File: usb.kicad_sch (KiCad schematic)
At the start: 24 parts, among them J4 CONN_02X03, U6 FT231XQ, Y1 FNETHE025

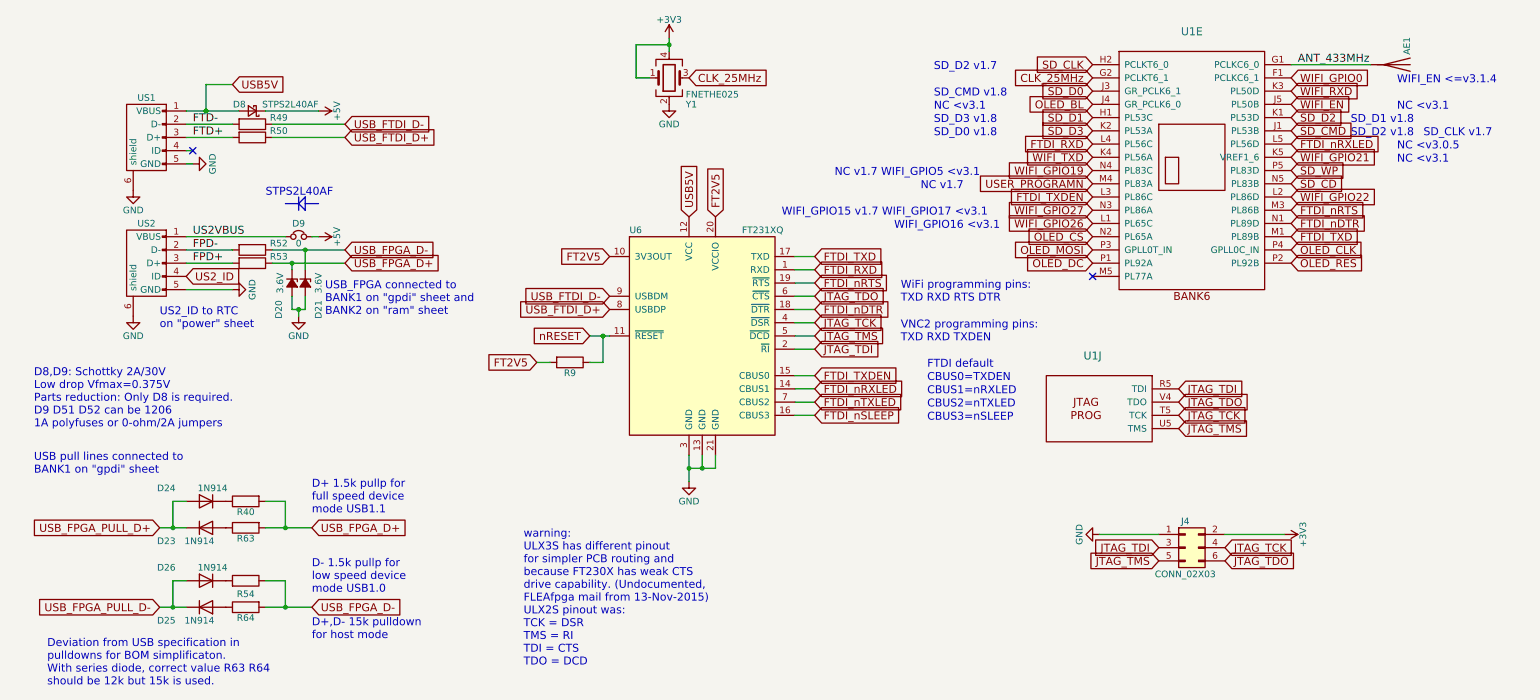
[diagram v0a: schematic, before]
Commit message: Adding USB-C
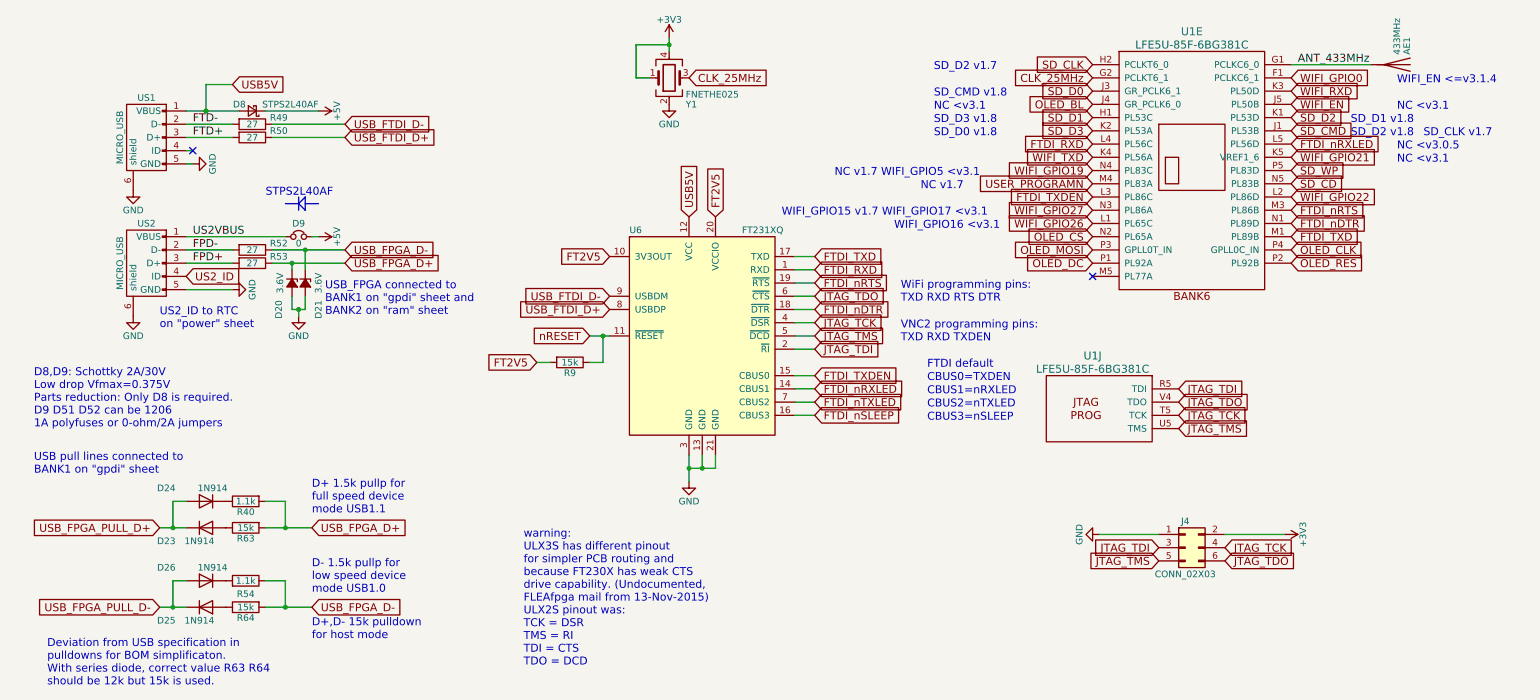
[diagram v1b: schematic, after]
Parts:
- AE1: value (none) -> 433MHz; footprint (none) -> USB-C:1013706200021LF
- J4: footprint Socket_Strips:Socket_Strip_Straight_2x03 -> Connector_PinSocket_2.54mm:PinSocket_2x03_P2.54mm_Vertical_SMD
- R40, R54: value (none) -> 1.1k; footprint (none) -> Resistor_SMD:R_0603_1608Metric
- R49, R50, R52, R53: value (none) -> 27; footprint (none) -> Resistor_SMD:R_0603_1608Metric
- R63, R64, R9: value (none) -> 15k; footprint (none) -> Resistor_SMD:R_0603_1608Metric
- U1: value (none) -> LFE5U-85F-6BG381C; footprint (none) -> lfe5bg381:BGA-381_pitch0.8mm_dia0.4mm
- US1, US2: value (none) -> MICRO_USB; footprint (none) -> usb_otg:USB-MICRO-B-FCI-10118192-0001LF
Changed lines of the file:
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@@
   (title_block
     (title "ULX3S")
-    (rev "1.0.10")
+    (date "2023-01-19")
+    (rev "3.1.8")
     (company "EMARD")
     (comment 1 "USB serial and JTAG")
@@
     (in_bom yes) (on_board yes)
     (property "Reference" "US1" (id 0) (at 38.1 40.64 90))
-    (property "Value" "" (id 1) (at 33.02 48.26 0))
-    (property "Footprint" "" (id 2) (at 40.64 46.99 90)
+    (property "Value" "MICRO_USB" (id 1) (at 33.02 48.26 0))
+    (property "Footprint" "usb_otg:USB-MICRO-B-FCI-10118192-0001LF" (id 2) (at 40.64 46.99 90)
       (effects (font (size 1.27 1.27)) hide)
     )
@@
     (in_bom yes) (on_board yes)
     (property "Reference" "US2" (id 0) (at 38.1 64.77 90))
-    (property "Value" "" (id 1) (at 33.02 72.39 0))
-    (property "Footprint" "" (id 2) (at 40.64 71.12 90)
+    (property "Value" "MICRO_USB" (id 1) (at 33.02 72.39 0))
+    (property "Footprint" "usb_otg:USB-MICRO-B-FCI-10118192-0001LF" (id 2) (at 40.64 71.12 90)
       (effects (font (size 1.27 1.27)) hide)
     )
@@
     (in_bom yes) (on_board yes)
     (property "Reference" "R9" (id 0) (at 119.38 93.472 90))
-    (property "Value" "" (id 1) (at 119.38 91.44 90))
-    (property "Footprint" "" (id 2) (at 119.38 89.662 90)
+    (property "Value" "15k" (id 1) (at 119.38 91.44 90))
+    (property "Footprint" "Resistor_SMD:R_0603_1608Metric" (id 2) (at 119.38 89.662 90)
       (effects (font (size 1.27 1.27)) hide)
     )
@@
     (in_bom yes) (on_board yes)
     (property "Reference" "R40" (id 0) (at 57.15 120.142 90))
-    (property "Value" "" (id 1) (at 57.15 118.11 90))
-    (property "Footprint" "" (id 2) (at 57.15 116.332 90)
+    (property "Value" "1.1k" (id 1) (at 57.15 118.11 90))
+    (property "Footprint" "Resistor_SMD:R_0603_1608Metric" (id 2) (at 57.15 116.332 90)
       (effects (font (size 1.27 1.27)) hide)
     )
@@
     (property "Reference" "J4" (id 0) (at 237.49 121.92 0))
     (property "Value" "CONN_02X03" (id 1) (at 237.49 132.08 0))
-    (property "Footprint" "Socket_Strips:Socket_Strip_Straight_2x03" (id 2) (at 237.49 157.48 0)
+    (property "Footprint" "Connector_PinSocket_2.54mm:PinSocket_2x03_P2.54mm_Vertical_SMD" (id 2) (at 237.49 157.48 0)
       (effects (font (size 1.27 1.27)) hide)
     )
@@
     (in_bom yes) (on_board yes)
     (property "Reference" "R49" (id 0) (at 63.5 44.45 90))
-    (property "Value" "" (id 1) (at 58.42 45.72 90))
-    (property "Footprint" "" (id 2) (at 58.42 43.942 90)
+    (property "Value" "27" (id 1) (at 58.42 45.72 90))
+    (property "Footprint" "Resistor_SMD:R_0603_1608Metric" (id 2) (at 58.42 43.942 90)
       (effects (font (size 1.27 1.27)) hide)
     )
@@
     (in_bom yes) (on_board yes)
     (property "Reference" "R50" (id 0) (at 63.5 46.99 90))
-    (property "Value" "" (id 1) (at 58.42 48.26 90))
-    (property "Footprint" "" (id 2) (at 58.42 46.482 90)
+    (property "Value" "27" (id 1) (at 58.42 48.26 90))
+    (property "Footprint" "Resistor_SMD:R_0603_1608Metric" (id 2) (at 58.42 46.482 90)
       (effects (font (size 1.27 1.27)) hide)
     )
@@
     (in_bom yes) (on_board yes)
     (property "Reference" "R52" (id 0) (at 63.5 68.58 90))
-    (property "Value" "" (id 1) (at 58.42 69.85 90))
-    (property "Footprint" "" (id 2) (at 58.42 68.072 90)
+    (property "Value" "27" (id 1) (at 58.42 69.85 90))
+    (property "Footprint" "Resistor_SMD:R_0603_1608Metric" (id 2) (at 58.42 68.072 90)
       (effects (font (size 1.27 1.27)) hide)
     )
@@
     (in_bom yes) (on_board yes)
     (property "Reference" "R53" (id 0) (at 63.5 71.12 90))
-    (property "Value" "" (id 1) (at 58.42 72.39 90))
-    (property "Footprint" "" (id 2) (at 58.42 70.612 90)
+    (property "Value" "27" (id 1) (at 58.42 72.39 90))
+    (property "Footprint" "Resistor_SMD:R_0603_1608Metric" (id 2) (at 58.42 70.612 90)
       (effects (font (size 1.27 1.27)) hide)
     )
@@
       (effects (font (size 1.27 1.27)) (justify right))
     )
-    (property "Value" "" (id 1) (at 278.13 32.385 0)
+    (property "Value" "433MHz" (id 1) (at 278.13 32.385 0)
       (effects (font (size 1.27 1.27)) (justify right))
     )
-    (property "Footprint" "" (id 2) (at 278.13 34.29 0)
+    (property "Footprint" "USB-C:1013706200021LF" (id 2) (at 278.13 34.29 0)
       (effects (font (size 1.27 1.27)) hide)
     )
@@
     (in_bom yes) (on_board yes)
     (property "Reference" "R54" (id 0) (at 57.15 135.89 90))
-    (property "Value" "" (id 1) (at 57.15 133.35 90))
-    (property "Footprint" "" (id 2) (at 57.15 135.128 90)
+    (property "Value" "1.1k" (id 1) (at 57.15 133.35 90))
+    (property "Footprint" "Resistor_SMD:R_0603_1608Metric" (id 2) (at 57.15 135.128 90)
       (effects (font (size 1.27 1.27)) hide)
     )
@@
       (effects (font (size 1.524 1.524)))
     )
-    (property "Value" "" (id 1) (at 238.76 30.48 0)
+    (property "Value" "LFE5U-85F-6BG381C" (id 1) (at 238.76 30.48 0)
       (effects (font (size 1.524 1.524)))
     )
-    (property "Footprint" "" (id 2) (at 212.09 27.94 0)
+    (property "Footprint" "lfe5bg381:BGA-381_pitch0.8mm_dia0.4mm" (id 2) (at 212.09 27.94 0)
       (effects (font (size 1.524 1.524)) hide)
     )
@@
       (effects (font (size 1.524 1.524)))
     )
-    (property "Value" "" (id 1) (at 219.71 92.71 0)
+    (property "Value" "LFE5U-85F-6BG381C" (id 1) (at 219.71 92.71 0)
       (effects (font (size 1.524 1.524)))
     )
-    (property "Footprint" "" (id 2) (at 245.11 76.2 0)
+    (property "Footprint" "lfe5bg381:BGA-381_pitch0.8mm_dia0.4mm" (id 2) (at 245.11 76.2 0)
       (effects (font (size 1.524 1.524)) hide)
     )
@@
     (in_bom yes) (on_board yes)
     (property "Reference" "R63" (id 0) (at 57.15 125.222 90))
-    (property "Value" "" (id 1) (at 57.15 123.19 90))
-    (property "Footprint" "" (id 2) (at 57.15 121.412 90)
+    (property "Value" "15k" (id 1) (at 57.15 123.19 90))
+    (property "Footprint" "Resistor_SMD:R_0603_1608Metric" (id 2) (at 57.15 121.412 90)
       (effects (font (size 1.27 1.27)) hide)
     )
@@
     (in_bom yes) (on_board yes)
     (property "Reference" "R64" (id 0) (at 57.15 140.462 90))
-    (property "Value" "" (id 1) (at 57.15 138.43 90))
-    (property "Footprint" "" (id 2) (at 57.15 136.652 90)
-      (effects (font (size 1.27 1.27)) hide)
-    )
+    (property "Value" "15k" (id 1) (at 57.15 138.43 90))
+    (property "Footprint" "Resistor_SMD:R_0603_1608Metric" (id 2) (at 57.15 136.652 90)
+      (effects (font (size 1.27 1.27)) hide)
+    )

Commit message: Adding 1.2V option - fixing 3D view
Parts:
- J4: footprint Connector_PinSocket_2.54mm:PinSocket_2x03_P2.54mm_Vertical_SMD -> Connector_PinSocket_1.27mm:PinSocket_2x03_P1.27mm_Vertical
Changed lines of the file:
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@@
     (property "Reference" "J4" (id 0) (at 237.49 121.92 0))
     (property "Value" "CONN_02X03" (id 1) (at 237.49 132.08 0))
-    (property "Footprint" "Connector_PinSocket_2.54mm:PinSocket_2x03_P2.54mm_Vertical_SMD" (id 2) (at 237.49 157.48 0)
+    (property "Footprint" "Connector_PinSocket_1.27mm:PinSocket_2x03_P1.27mm_Vertical" (id 2) (at 237.49 157.48 0)
       (effects (font (size 1.27 1.27)) hide)
     )
